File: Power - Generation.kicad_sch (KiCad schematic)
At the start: 34 parts, among them Q1 AO3400A, Q2 AO3400A, Q3 SI2301CDS-T1-GE3, SW8 Button SPST SMD Tactile Switch, U4 AMS1117-3.3, U5 TPS61252DSG

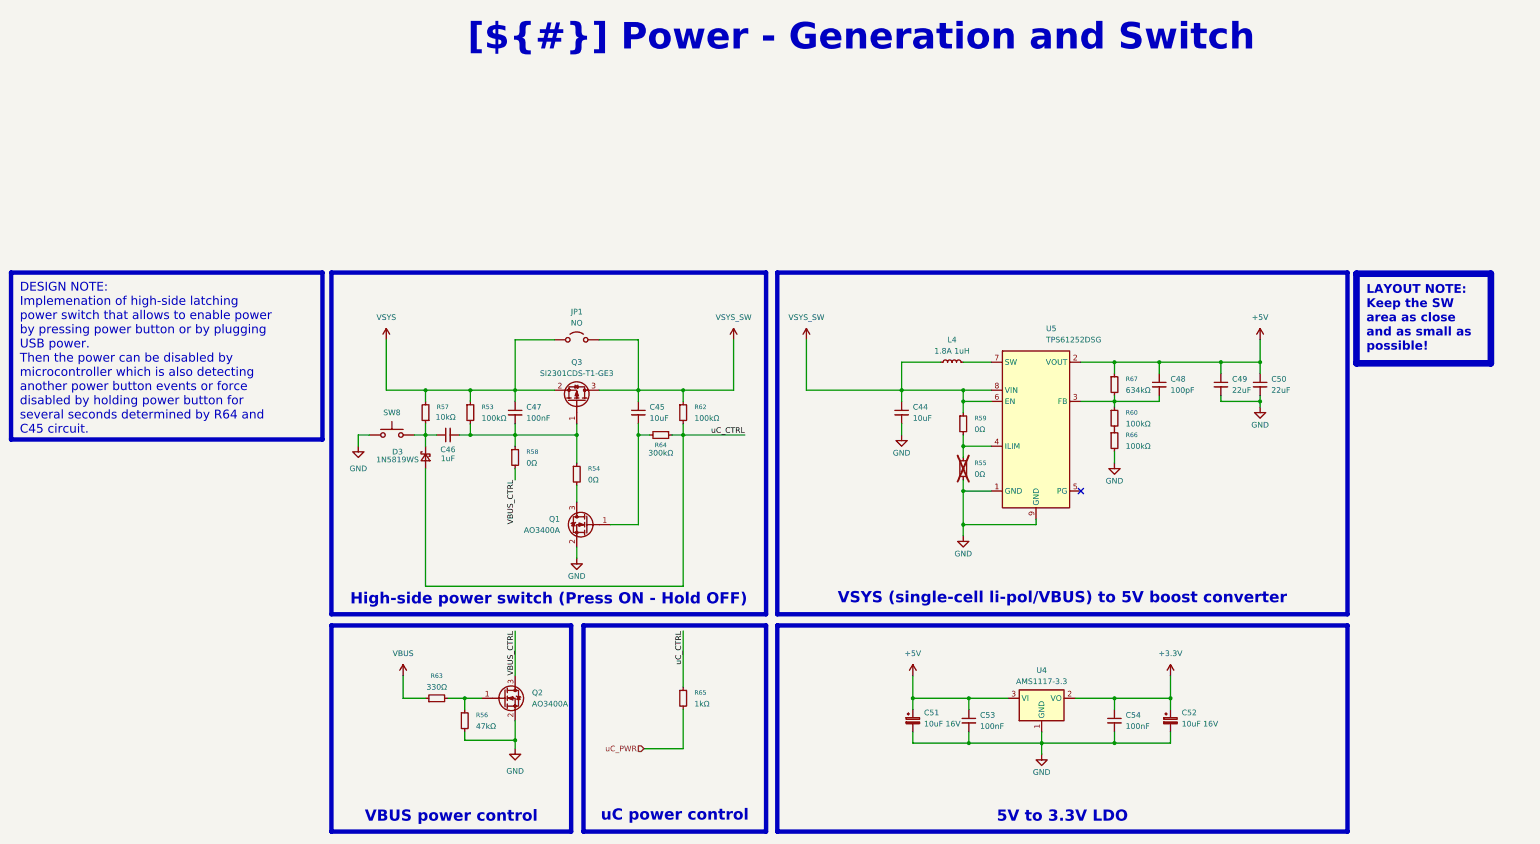
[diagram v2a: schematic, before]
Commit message: added fiducal markers, mounting holes, testpoints
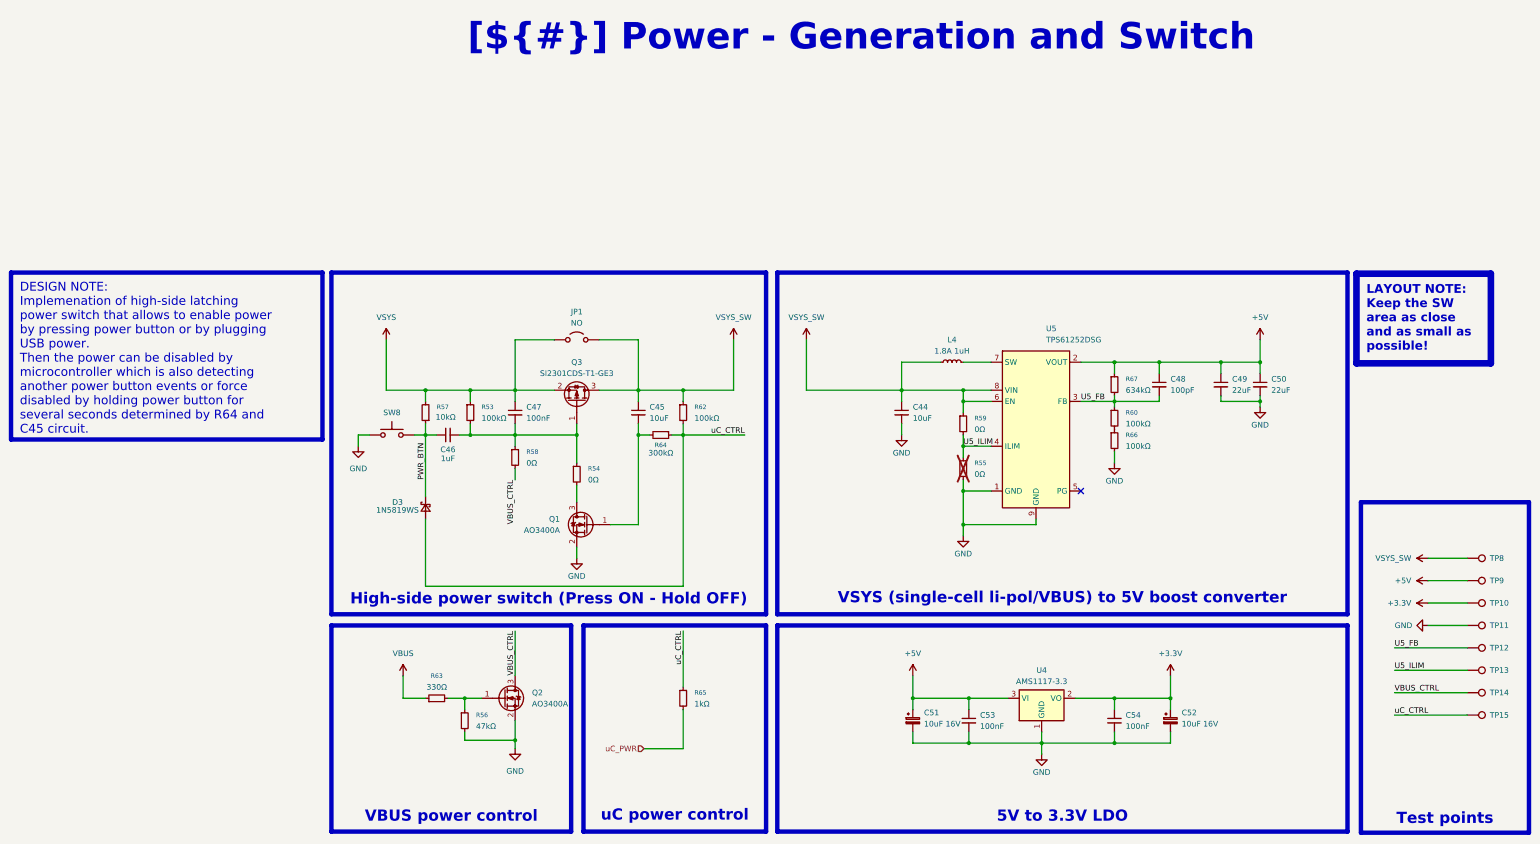
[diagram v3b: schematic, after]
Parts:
- added TP10, TP11, TP12, TP13, TP14, TP15, TP8, TP9: TestPoint, 0_pads:TestPoint_Pad_D0.4mm_Back, symbol Connector:TestPoint
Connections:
- net +3.3V: now also TP10.1
- net +5V: now also TP9.1
- net GND: now also TP11.1
- net VBUS_CTRL: now also TP14.1
- net VSYS_SW: now also TP8.1
- net uC_CTRL: now also TP15.1
- net U5_FB: now reaches C48.2, R60.1, R67.2, U5.3 (FB)
- net U5_FB: now also TP12.1
- net U5_ILIM: now reaches R55.1, R59.2, U5.4 (ILIM)
- net U5_ILIM: now also TP13.1
- net PWR_BTN: now reaches C46.1, D3.1 (K), R57.1, SW8.1
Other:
- moved on the sheet: D3

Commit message: test points, colors, drc
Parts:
- TP10, TP11, TP12, TP13, TP14, TP15, TP8, TP9: footprint 0_pads:TestPoint_Pad_D0.4mm_Back -> 0_pads:TestPoint_Pad_D0.5mm_Back
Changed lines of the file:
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@@
 		(polyline
 			(pts
-				(xy 287.02 102.87) (xy 307.34 102.87) (xy 307.34 90.17) (xy 287.02 90.17)
+				(xy 214.884 100.33) (xy 214.884 107.696) (xy 229.87 107.696) (xy 229.87 100.33) (xy 246.38 100.33)
+				(xy 246.38 85.09) (xy 214.884 85.09)
 			)
 			(stroke
@@
 		(polyline
 			(pts
-				(xy 214.884 100.33) (xy 214.884 107.696) (xy 229.87 107.696) (xy 229.87 100.33) (xy 246.38 100.33)
-				(xy 246.38 85.09) (xy 214.884 85.09)
+				(xy 287.02 102.87) (xy 307.34 102.87) (xy 307.34 90.17) (xy 287.02 90.17)
 			)
 			(stroke
@@
 			)
 		)
-		(property "Footprint" "0_pads:TestPoint_Pad_D0.4mm_Back"
+		(property "Footprint" "0_pads:TestPoint_Pad_D0.5mm_Back"
 			(at 346.71 177.8 0)
 			(effects
@@
 			)
 		)
-		(property "Footprint" "0_pads:TestPoint_Pad_D0.4mm_Back"
+		(property "Footprint" "0_pads:TestPoint_Pad_D0.5mm_Back"
 			(at 346.71 167.64 0)
 			(effects
@@
 			)
 		)
-		(property "Footprint" "0_pads:TestPoint_Pad_D0.4mm_Back"
+		(property "Footprint" "0_pads:TestPoint_Pad_D0.5mm_Back"
 			(at 346.71 142.24 0)
 			(effects
@@
 			)
 		)
-		(property "Footprint" "0_pads:TestPoint_Pad_D0.4mm_Back"
+		(property "Footprint" "0_pads:TestPoint_Pad_D0.5mm_Back"
 			(at 346.71 152.4 0)
 			(effects
@@
 			)
 		)
-		(property "Footprint" "0_pads:TestPoint_Pad_D0.4mm_Back"
+		(property "Footprint" "0_pads:TestPoint_Pad_D0.5mm_Back"
 			(at 346.71 162.56 0)
 			(effects
@@
 			)
 		)
-		(property "Footprint" "0_pads:TestPoint_Pad_D0.4mm_Back"
+		(property "Footprint" "0_pads:TestPoint_Pad_D0.5mm_Back"
 			(at 346.71 157.48 0)
 			(effects
@@
 			)
 		)
-		(property "Footprint" "0_pads:TestPoint_Pad_D0.4mm_Back"
+		(property "Footprint" "0_pads:TestPoint_Pad_D0.5mm_Back"
 			(at 346.71 172.72 0)
 			(effects
@@
 			)
 		)
-		(property "Footprint" "0_pads:TestPoint_Pad_D0.4mm_Back"
+		(property "Footprint" "0_pads:TestPoint_Pad_D0.5mm_Back"
 			(at 346.71 147.32 0)
 			(effects

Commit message: designator chagnes and cleanup silkscreen
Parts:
- C44, C45: LCSC PN (none) -> C15850
- C46: LCSC PN (none) -> C15849
- C47, C53, C54: LCSC PN (none) -> C1525
- C48: LCSC PN (none) -> C14858
- C49, C50: LCSC PN (none) -> C45783
- C51, C52: LCSC PN (none) -> C7171
- D3: LCSC PN (none) -> C191023
- L4: LCSC PN (none) -> C354573
- Q1, Q2: LCSC PN (none) -> C20917
- Q3: LCSC PN (none) -> C10487
- R53, R60, R62, R66: LCSC PN (none) -> C25741
- R54, R55, R58, R59: LCSC PN (none) -> C17168
- R56: LCSC PN (none) -> C25792
- R57: LCSC PN (none) -> C25744
- R63: LCSC PN (none) -> C25104
- R64: LCSC PN (none) -> C23024
- R65: LCSC PN (none) -> C11702
- R67: LCSC PN (none) -> C321583
- SW8: LCSC PN (none) -> C720477
- U5: LCSC PN (none) -> C128617
